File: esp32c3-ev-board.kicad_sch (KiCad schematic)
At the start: 46 parts, among them IC1 ESP32-C3FH4, IC2 W25Q128JVSIQ, IC3 ACS711EEXTK-31AB-T, J1 Battery Neg(Series), J2 Battery Pos, J3 USB_C_Receptacle_USB2.0, SW1 SW_DPST_x2, U1 USBLC6-2SC6, U2 LM2576HVS-3.3, Y1 40MHZ

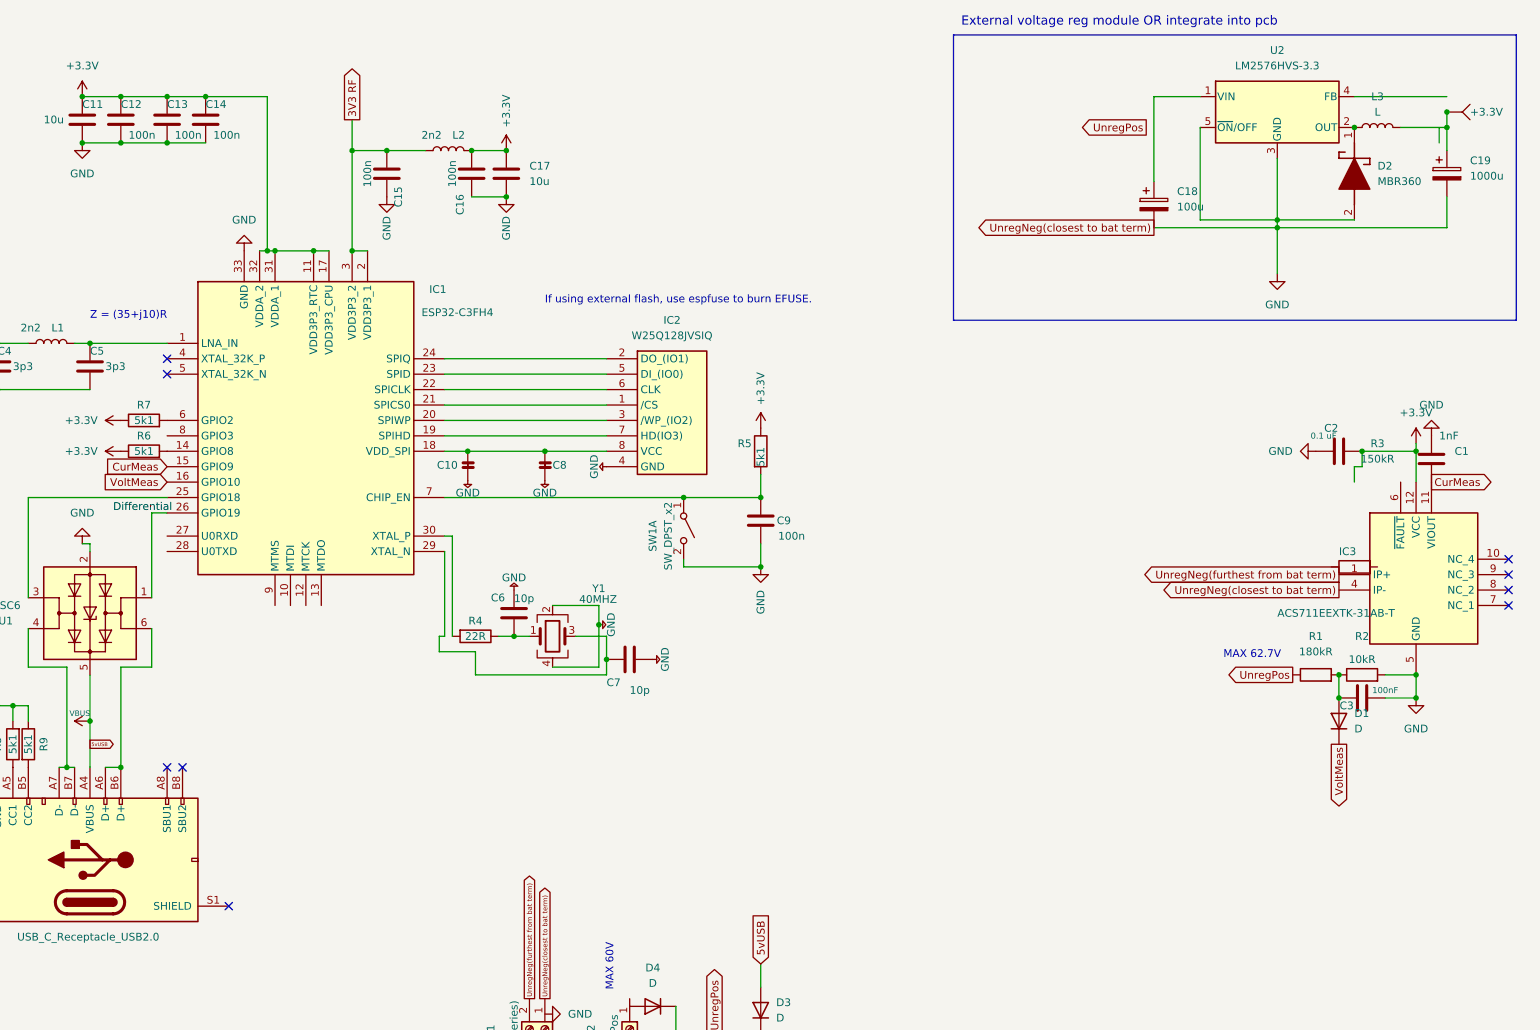
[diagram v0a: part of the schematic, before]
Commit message: added LEDs
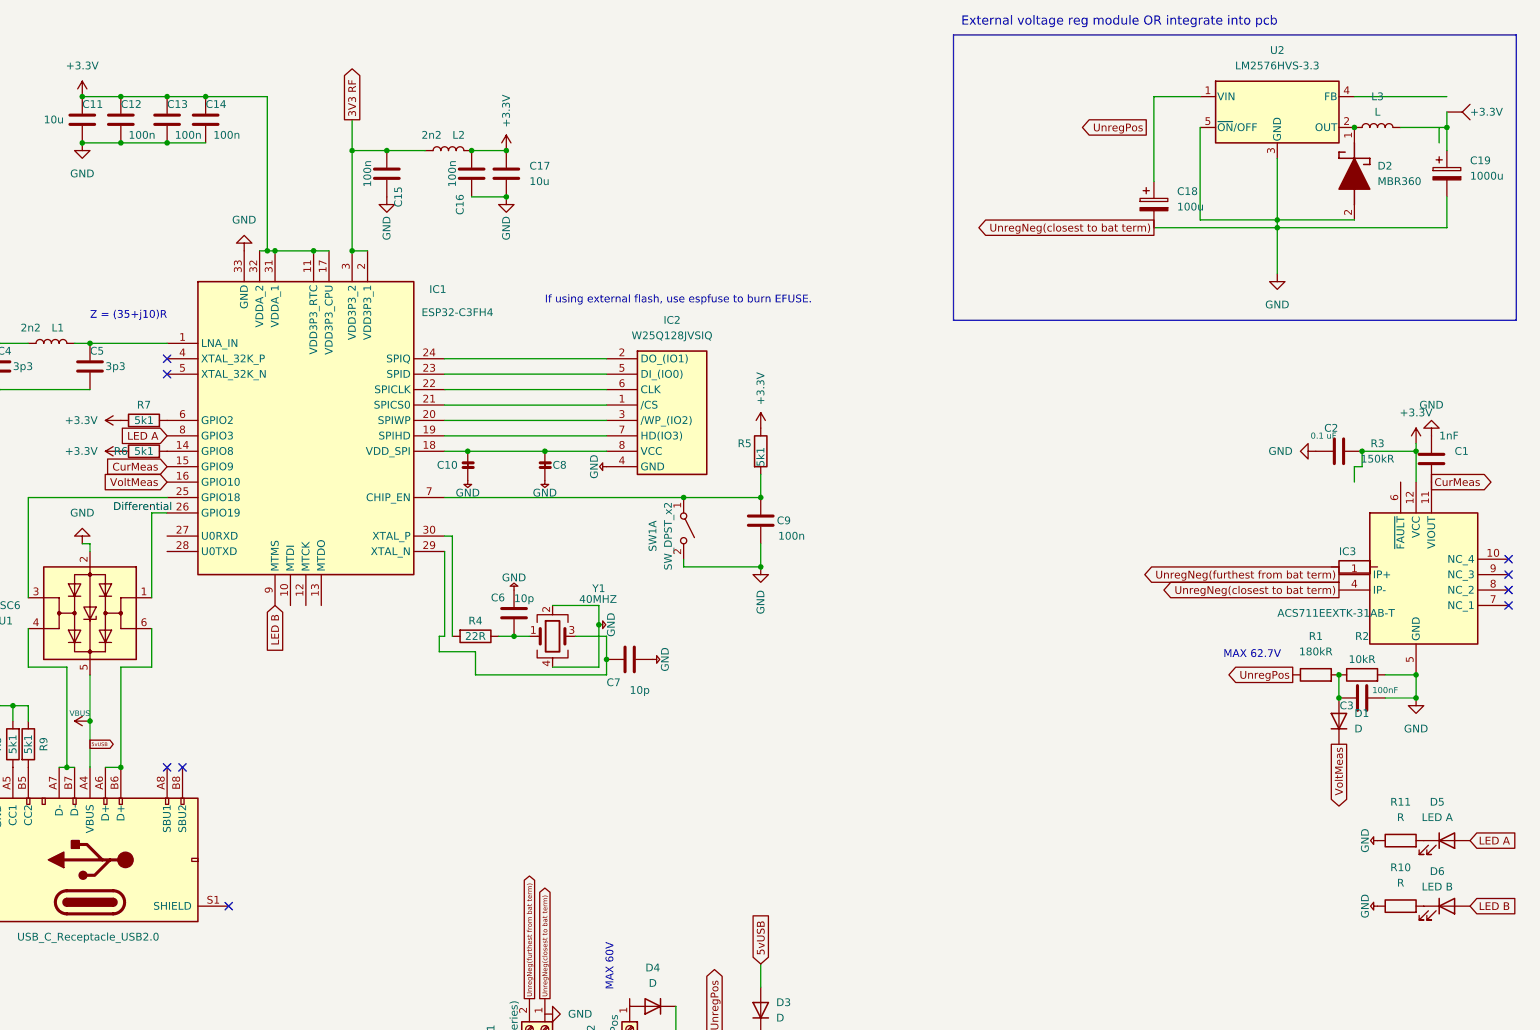
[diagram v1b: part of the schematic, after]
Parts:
- added D5: LED A, symbol Device:LED
- added D6: LED B, symbol Device:LED
- added R10, R11: R, symbol Device:R
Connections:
- net GND: now also R10.1, R11.1
- net LED A: now reaches IC1.8 (GPIO3)
- net LED A: now also D5.2 (A)
- net LED B: now reaches IC1.9 (MTMS)
- net LED B: now also D6.2 (A)
- new net: D6.1 (K), R10.2
- new net: D5.1 (K), R11.2
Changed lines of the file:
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@@
   (junction (at 77.47 54.61) (diameter 0) (color 0 0 0 0)
-  )
-  (junction (at 271.78 31.75) (diameter 0) (color 0 0 0 0)
   )
   (junction (at 91.44 38.1) (diameter 0) (color 0 0 0 0)
@@
     (effects (font (size 1.27 1.27)) (justify left bottom))
   )
+  (global_label "LED B" (shape input) (at 78.74 113.03 270) (fields_autoplaced)
+    (effects (font (size 1.27 1.27)) (justify right))
+    (property "Intersheetrefs" "${INTERSHEET_REFS}" (at 78.74 121.6205 90)
+      (effects (font (size 1.27 1.27)) (justify right) hide)
+    )
+  )
   (global_label "UnregNeg(furthest from bat term)" (shape output) (at 254 107.95 180) (fields_autoplaced)
     (effects (font (size 1.27 1.27)) (justify right))
@@
     )
   )
+  (global_label "LED A" (shape input) (at 60.96 85.09 180) (fields_autoplaced)
+    (effects (font (size 1.27 1.27)) (justify right))
+    (property "Intersheetrefs" "${INTERSHEET_REFS}" (at 52.5509 85.09 0)
+      (effects (font (size 1.27 1.27)) (justify right) hide)
+    )
+  )
   (global_label "VoltMeas" (shape output) (at 254 135.89 270) (fields_autoplaced)
     (effects (font (size 1.27 1.27)) (justify right))
@@
     )
   )
+  (global_label "LED B" (shape input) (at 275.59 162.56 0) (fields_autoplaced)
+    (effects (font (size 1.27 1.27)) (justify left))
+    (property "Intersheetrefs" "${INTERSHEET_REFS}" (at 284.1805 162.56 0)
+      (effects (font (size 1.27 1.27)) (justify left) hide)
+    )
+  )
   (global_label "CurMeas" (shape output) (at 269.24 92.71 0) (fields_autoplaced)
     (effects (font (size 1.27 1.27)) (justify left))
@@
     (property "Intersheetrefs" "${INTERSHEET_REFS}" (at 49.6292 92.71 0)
       (effects (font (size 1.27 1.27)) (justify right) hide)
+    )
+  )
+  (global_label "LED A" (shape input) (at 275.59 151.765 0) (fields_autoplaced)
+    (effects (font (size 1.27 1.27)) (justify left))
+    (property "Intersheetrefs" "${INTERSHEET_REFS}" (at 283.9991 151.765 0)
+      (effects (font (size 1.27 1.27)) (justify left) hide)
     )
   )
@@
   (symbol (lib_id "Device:R") (at 57.15 87.63 90) (unit 1)
     (in_bom yes) (on_board yes) (dnp no)
-    (property "Reference" "R6" (at 57.15 85.09 90)
+    (property "Reference" "R6" (at 53.34 87.63 90)
       (effects (font (size 1.27 1.27)))
     )
@@
     )
   )
+  (symbol (lib_id "Device:R") (at 264.16 162.56 90) (unit 1)
+    (in_bom yes) (on_board yes) (dnp no) (fields_autoplaced)
+    (property "Reference" "R10" (at 264.16 156.21 90)
+      (effects (font (size 1.27 1.27)))
+    )
+    (property "Value" "R" (at 264.16 158.75 90)
+      (effects (font (size 1.27 1.27)))
+    )
+    (property "Footprint" "" (at 264.16 164.338 90)
+      (effects (font (size 1.27 1.27)) hide)
+    )
+    (property "Datasheet" "~" (at 264.16 162.56 0)
+      (effects (font (size 1.27 1.27)) hide)
+    )
+    (pin "1")
+    (pin "2")
+    (instances
+      (project "esp32c3-ev-board"
+        (path "/f5da1fcc-93b5-4c63-bb34-c18c11bc243c"
+          (reference "R10") (unit 1)
+        )
+      )
+    )
+  )
   (symbol (lib_id "power:+3.3V") (at 53.34 87.63 90) (unit 1)
     (in_bom yes) (on_board yes) (dnp no) (fields_autoplaced)
@@
         (path "/f5da1fcc-93b5-4c63-bb34-c18c11bc243c"
           (reference "#PWR03") (unit 1)
+        )
+      )
+    )
+  )
+  (symbol (lib_id "Device:LED") (at 271.78 162.56 0) (unit 1)
+    (in_bom yes) (on_board yes) (dnp no) (fields_autoplaced)
+    (property "Reference" "D6" (at 270.1925 156.845 0)
+      (effects (font (size 1.27 1.27)))
+    )
+    (property "Value" "LED B" (at 270.1925 159.385 0)
+      (effects (font (size 1.27 1.27)))
+    )
+    (property "Footprint" "" (at 271.78 162.56 0)
+      (effects (font (size 1.27 1.27)) hide)
+    )
+    (property "Datasheet" "~" (at 271.78 162.56 0)
+      (effects (font (size 1.27 1.27)) hide)
+    )
+    (pin "1")
+    (pin "2")
+    (instances
+      (project "esp32c3-ev-board"
+        (path "/f5da1fcc-93b5-4c63-bb34-c18c11bc243c"
+          (reference "D6") (unit 1)
         )
       )
@@
     )
   )
+  (symbol (lib_id "Device:LED") (at 271.78 151.765 0) (unit 1)
+    (in_bom yes) (on_board yes) (dnp no) (fields_autoplaced)
+    (property "Reference" "D5" (at 270.1925 145.415 0)
+      (effects (font (size 1.27 1.27)))
+    )
+    (property "Value" "LED A" (at 270.1925 147.955 0)
+      (effects (font (size 1.27 1.27)))
+    )
+    (property "Footprint" "" (at 271.78 151.765 0)
+      (effects (font (size 1.27 1.27)) hide)
+    )
+    (property "Datasheet" "~" (at 271.78 151.765 0)
+      (effects (font (size 1.27 1.27)) hide)
+    )
+    (pin "1")
+    (pin "2")
+    (instances
+      (project "esp32c3-ev-board"
+        (path "/f5da1fcc-93b5-4c63-bb34-c18c11bc243c"
+          (reference "D5") (unit 1)
+        )
+      )
+    )
+  )
   (symbol (lib_id "Device:L") (at 41.91 69.85 90) (unit 1)
     (in_bom yes) (on_board yes) (dnp no)
@@
         (path "/f5da1fcc-93b5-4c63-bb34-c18c11bc243c"
           (reference "C4") (unit 1)
+        )
+      )
+    )
+  )
+  (symbol (lib_name "GND_1") (lib_id "power:GND") (at 260.35 162.56 270) (unit 1)
+    (in_bom yes) (on_board yes) (dnp no)
+    (property "Reference" "#PWR029" (at 254 162.56 0)
+      (effects (font (size 1.27 1.27)) hide)
+    )
+    (property "Value" "GND" (at 258.318 162.56 0)
+      (effects (font (size 1.27 1.27)))
+    )
+    (property "Footprint" "" (at 260.35 162.56 0)
+      (effects (font (size 1.27 1.27)) hide)
+    )
+    (property "Datasheet" "" (at 260.35 162.56 0)
+      (effects (font (size 1.27 1.27)) hide)
+    )
+    (pin "1")
+    (instances
+      (project "esp32c3-ev-board"
+        (path "/f5da1fcc-93b5-4c63-bb34-c18c11bc243c"
+          (reference "#PWR029") (unit 1)
         )
       )
@@
     )
   )
+  (symbol (lib_id "Device:R") (at 264.16 151.765 90) (unit 1)
+    (in_bom yes) (on_board yes) (dnp no) (fields_autoplaced)
+    (property "Reference" "R11" (at 264.16 145.415 90)
+      (effects (font (size 1.27 1.27)))
+    )
+    (property "Value" "R" (at 264.16 147.955 90)
+      (effects (font (size 1.27 1.27)))
+    )
+    (property "Footprint" "" (at 264.16 153.543 90)
+      (effects (font (size 1.27 1.27)) hide)
+    )
+    (property "Datasheet" "~" (at 264.16 151.765 0)
+      (effects (font (size 1.27 1.27)) hide)
+    )
+    (pin "1")
+    (pin "2")
+    (instances
+      (project "esp32c3-ev-board"
+        (path "/f5da1fcc-93b5-4c63-bb34-c18c11bc243c"
+          (reference "R11") (unit 1)
+        )
+      )
+    )
+  )
   (symbol (lib_id "power:GND") (at 46.99 102.87 180) (unit 1)
     (in_bom yes) (on_board yes) (dnp no) (fields_autoplaced)
@@
         )
       )
+    )
+  )
+  (symbol (lib_name "GND_1") (lib_id "power:GND") (at 260.35 151.765 270) (unit 1)
+    (in_bom yes) (on_board yes) (dnp no)
+    (property "Reference" "#PWR028" (at 254 151.765 0)
+      (effects (font (size 1.27 1.27)) hide)
+    )
+    (property "Value" "GND" (at 258.318 151.765 0)
+      (effects (font (size 1.27 1.27)))
+    )
+    (property "Footprint" "" (at 260.35 151.765 0)
+      (effects (font (size 1.27 1.27)) hide)
+    )
+    (property "Datasheet" "" (at 260.35 151.765 0)
+      (effects (font (size 1.27 1.27)) hide)
+    )
+    (pin "1")
+    (instances
+      (project "esp32c3-ev-board"
+        (path "/f5da1fcc-93b5-4c63-bb34-c18c11bc243c"
+          (reference "#PWR028") (unit 1)
+        )
+      )

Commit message: rearranging schematic
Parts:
- removed C9: 100n, symbol Device:C
- removed R5: 5k1, symbol Device:R
- removed SW1: SW_DPST_x2, symbol Switch:SW_DPST_x2
- added C20, C21, C22, C23, C24: 100n, symbol Device:C
- added J4: Conn_01x04_Pin, symbol Connector:Conn_01x04_Pin
- added L4: 2n2, symbol Device:L
- added R12, R16: 5k1, symbol Device:R
- added R13: 1kR, symbol Device:R
- added R14, R15: 470R, symbol Device:R
- added SW2, SW3: SW_DPST_x2, symbol Switch:SW_DPST_x2
- added U3: USBLC6-2SC6, Package_TO_SOT_SMD:SOT-23-6, symbol Power_Protection:USBLC6-2SC6
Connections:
- net +3.3V: now also U2.4 (FB), R12.1, R13.2, R16.1
- net CurMeas: now also C20.1, R12.2, SW2.1 (A)
- net GND: now also C20.2, C23.2, C24.2, J4.3 (Pin_3), SW2.2 (B), SW3.2 (B), U3.2 (GND)
- net UnregPos: now also C18.1, U2.1 (VIN)
- net VBUS: now also C21.2, C23.1, J4.1 (Pin_1), U3.5 (VBUS); no longer J3.A4 (VBUS), U1.5 (VBUS)
- net USBDP: now reaches IC1.26 (GPIO19), U1.1 (I/O1)
- net USBDN: now reaches IC1.25 (GPIO18), U1.3 (I/O2)
- net at IC3.6 (~{FAULT}): now also R13.1
- net CHIPEN: now reaches IC1.7 (CHIP_EN)
- net CHIPEN: now also C24.1, R16.2, SW3.1 (A)
- net at D4.2 (A): now also J2.1 (Pin_1)
- net at IC1.27 (U0RXD): now also R14.2
- net at IC1.28 (U0TXD): now also R15.2
- new net: C22.1, L4.2
- new net: C21.1, L4.1
- new net: J4.2 (Pin_2), U3.4 (I/O2)
- new net: J4.4 (Pin_4), U3.6 (I/O1)
- new net 5vUSB: C22.2, J3.A4 (VBUS), U1.5 (VBUS)
- new net UARTRX: R14.1, U3.3 (I/O2)
- new net UARTTX: R15.1, U3.1 (I/O1)
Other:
- note added: "Buck Voltage Reg"
- note added: "Buttons"
- note added: "ESP32-C3FH4 + PCB Antenna"
- note added: "External module or integrate into circuit"
- note added: "LEDs"
- note added: "Periphirals"
- note added: "Sensors"
- note added: "Terminals"
- note added: "UART"
- note added: "USB C 2.0"
- note removed: "External voltage reg module OR integrate into pcb"
- moved on the sheet: ANT1, C1, C10, C11, C12, C13, C14, C15, C16, C17, C18, C19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

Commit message: change voltreg
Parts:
- removed C22: 100n, symbol Device:C
- removed D2: MBR360, DIOAD2860W130L840D505, symbol MBR360:MBR360
- removed L3: L, symbol Device:L
- removed R3: 150kR, symbol Device:R
- removed U2: LM2576HVS-3.3, Package_TO_SOT_SMD:TO-263-5_TabPin3, symbol Regulator_Switching:LM2576HVS-3.3
- added C9: 100n, symbol Device:C
- added IC4: SPX3819M5-L-3-3, SOT95P280X145-5N, symbol SPX3819M5-L-3-3:SPX3819M5-L-3-3
- added J5: Battery Pos, symbol Connector:Screw_Terminal_01x01
- added J6: Regulated Neg, symbol Connector:Screw_Terminal_01x01
- J2: value Battery Pos -> Regulated Pos
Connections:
- net 5vUSB: now also D3.1 (K), D4.1 (K)
- net GND: no longer C18.2, C19.2, IC3.4 (IP-), J1.1 (Pin_1)
- net UnregPos: now also J5.1 (Pin_1); no longer D3.1 (K), D4.1 (K)
- net VBUS: no longer C21.2
- net at L4.2: now also C9.1
- new net Reg Neg: J6.1 (Pin_1)
- new net Regulated Neg(closest to bat term): C18.2, C19.2
- new net UnregNeg(closest to bat term): IC3.4 (IP-), J1.1 (Pin_1)
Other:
- note added: "LDO Regulator"
- note added: "Use external voltage regulator to bring voltage down to 5v"
- note removed: "Buck Voltage Reg"
- note removed: "External module or integrate into circuit"

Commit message: volt reg work
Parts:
- removed C18: 100u, symbol Device:C_Polarized
- added C18: 10u, symbol Device:C
- added C22: 100n, symbol Device:C
- added D2: LED A, symbol Device:LED
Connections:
- net Regulated Neg(closest to bat term) is gone; now on net Reg Neg: C19.2
- net +3.3V: now also D2.1 (K)
- net 5vUSB: now also D3.2 (A); no longer D3.1 (K), D4.1 (K)
- net Reg Neg: now also C21.2, C9.2, IC4.2 (GND), C18.2, C22.2
- net VBUS: no longer D3.2 (A)
- net Reg Pos: now reaches C21.1, L4.1
- net Reg Pos: now also D3.1 (K), D4.1 (K)
- net at IC4.1 (VIN): now also C9.1, IC4.3 (EN), L4.2, C18.1
- net at IC4.4 (ADJ/BYP): now also C22.1, D2.2 (A)
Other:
- moved on the sheet: C21, C9, IC4, L4
